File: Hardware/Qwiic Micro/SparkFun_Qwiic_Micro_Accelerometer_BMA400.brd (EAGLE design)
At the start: 7.6 x 19.1 mm, 40 parts, among them J1 QWIIC_RIGHT_ANGLE, U1 BMA400

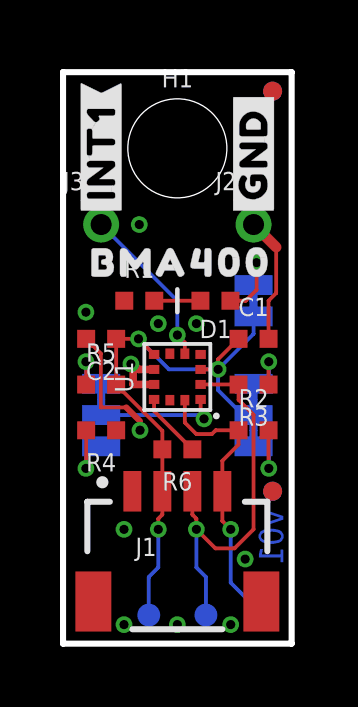
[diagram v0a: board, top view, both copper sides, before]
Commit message: Change default I2C address
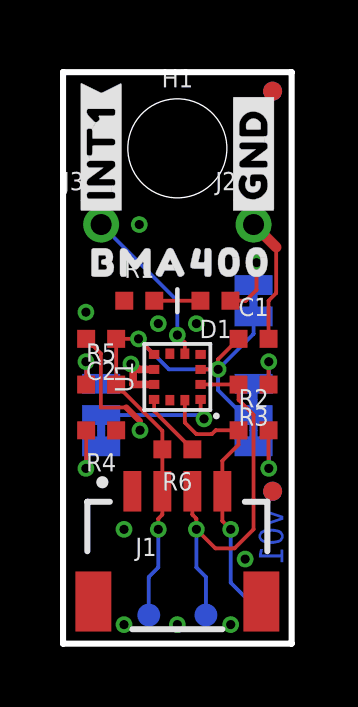
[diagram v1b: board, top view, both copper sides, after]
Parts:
- turned ADR to 270 degrees
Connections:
- net N$5: now also ADR.1; no longer ADR.3
- net N$6: now also ADR.3; no longer ADR.1
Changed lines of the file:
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@@
 </autorouter>
 <elements>
-<element name="ADR" library="SparkFun-Jumpers" package="SMT-JUMPER_3_1-NC_TRACE_SILK" package3d_urn="urn:adsk.eagle:package:39288/1" value="JUMPER-SMT_3_1-NC_TRACE_SILK" x="1.27" y="7.62" smashed="yes" rot="MR90">
-<attribute name="NAME" x="2.413" y="7.62" size="0.6096" layer="26" font="vector" ratio="20" rot="MR90" align="bottom-center"/>
-<attribute name="VALUE" x="0.127" y="7.62" size="0.6096" layer="28" font="vector" ratio="20" rot="MR90" align="top-center"/>
-</element>
 <element name="C1" library="SparkFun-Capacitors" package="0402-TIGHT" value="0.1uF" x="6.35" y="10.16" smashed="yes">
 <attribute name="NAME" x="6.35" y="10.922" size="0.6096" layer="25" font="vector" ratio="20" align="bottom-center"/>
@@
 <element name="U$10" library="output" package="#0X14#0" value="" x="1.27" y="6.223" smashed="yes" rot="MR90"/>
 <element name="U$11" library="output" package="#PWR#0" value="" x="5.588" y="11.43" smashed="yes" rot="MR0"/>
+<element name="ADR" library="SparkFun-Jumpers" package="SMT-JUMPER_3_1-NC_TRACE_SILK" package3d_urn="urn:adsk.eagle:package:39288/1" value="JUMPER-SMT_3_1-NC_TRACE_SILK" x="1.27" y="7.62" smashed="yes" rot="MR270">
+<attribute name="NAME" x="0.127" y="7.62" size="0.6096" layer="26" font="vector" ratio="20" rot="MR270" align="bottom-center"/>
+<attribute name="VALUE" x="2.413" y="7.62" size="0.6096" layer="28" font="vector" ratio="20" rot="MR270" align="top-center"/>
+</element>
 </elements>
 <signals>
@@
 <signal name="ADR">
 <contactref element="U1" pad="1"/>
-<contactref element="ADR" pad="2"/>
 <wire x1="4.585" y1="8.14" x2="4.585" y2="7.607" width="0.127" layer="1"/>
 <wire x1="4.585" y1="7.607" x2="4.699" y2="7.493" width="0.127" layer="1"/>
@@
 <wire x1="1.27" y1="7.62" x2="4.572" y2="7.62" width="0.127" layer="16"/>
 <wire x1="4.572" y1="7.62" x2="4.699" y2="7.493" width="0.127" layer="16"/>
+<contactref element="ADR" pad="2"/>
 </signal>
 <signal name="!CS!">
@@
 <signal name="N$5">
 <contactref element="R5" pad="1"/>
-<contactref element="ADR" pad="3"/>
 <wire x1="0.77" y1="8.636" x2="0.77" y2="9.39" width="0.127" layer="1"/>
 <wire x1="0.77" y1="9.39" x2="0.762" y2="9.398" width="0.127" layer="1"/>
@@
 <wire x1="0.762" y1="9.398" x2="0.762" y2="8.6614" width="0.127" layer="16"/>
 <wire x1="0.762" y1="8.6614" x2="1.27" y2="8.6614" width="0.127" layer="16"/>
+<contactref element="ADR" pad="1"/>
 </signal>
 <signal name="N$6">
 <contactref element="R4" pad="2"/>
-<contactref element="ADR" pad="1"/>
 <wire x1="0.77" y1="7.112" x2="0.77" y2="5.85" width="0.127" layer="1"/>
 <wire x1="0.77" y1="5.85" x2="0.762" y2="5.842" width="0.127" layer="1"/>
@@
 <wire x1="0.762" y1="5.842" x2="0.762" y2="6.5786" width="0.127" layer="16"/>
 <wire x1="0.762" y1="6.5786" x2="1.27" y2="6.5786" width="0.127" layer="16"/>
+<contactref element="ADR" pad="3"/>
 </signal>
 <signal name="N$1">
